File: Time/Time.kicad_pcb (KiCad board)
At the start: 2 copper layers, 100 x 100 mm, 24 parts, among them J1 Buss, J2 Timers, SW1 Slot, U1 DS12885, U2 74LS573, U3 74LS245, U4 GAL22V10, U5 74LS85, U6 MC6840, Y1 32.768KHz/6pF, Y2 32.768KHz

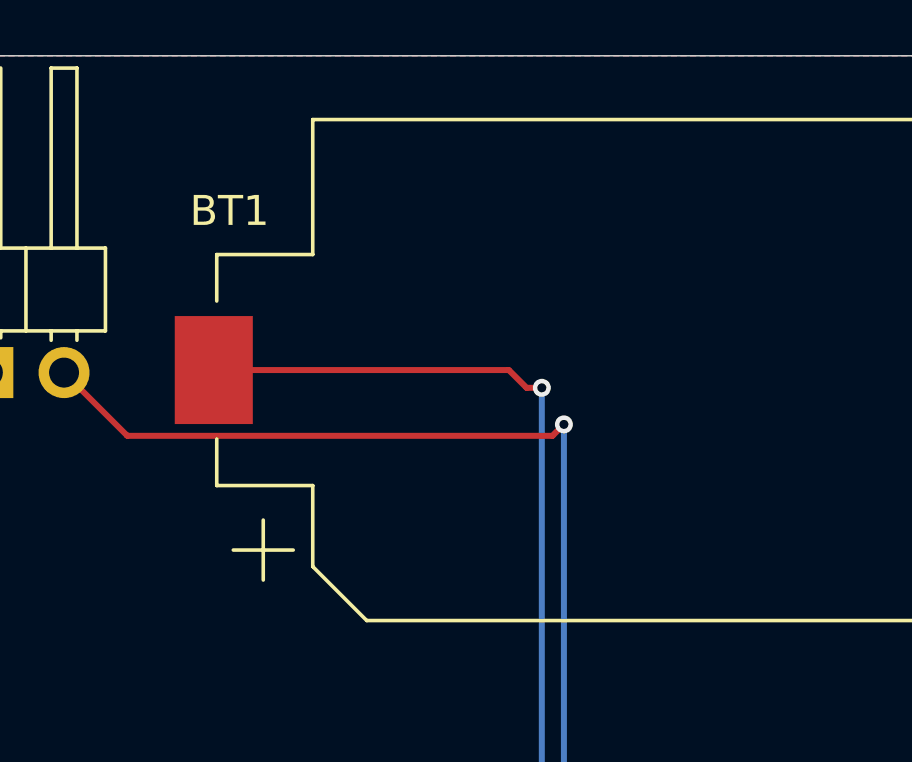
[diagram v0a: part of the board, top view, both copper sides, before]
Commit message: finish routing the coms board. add some step models to look at this thing in freecad
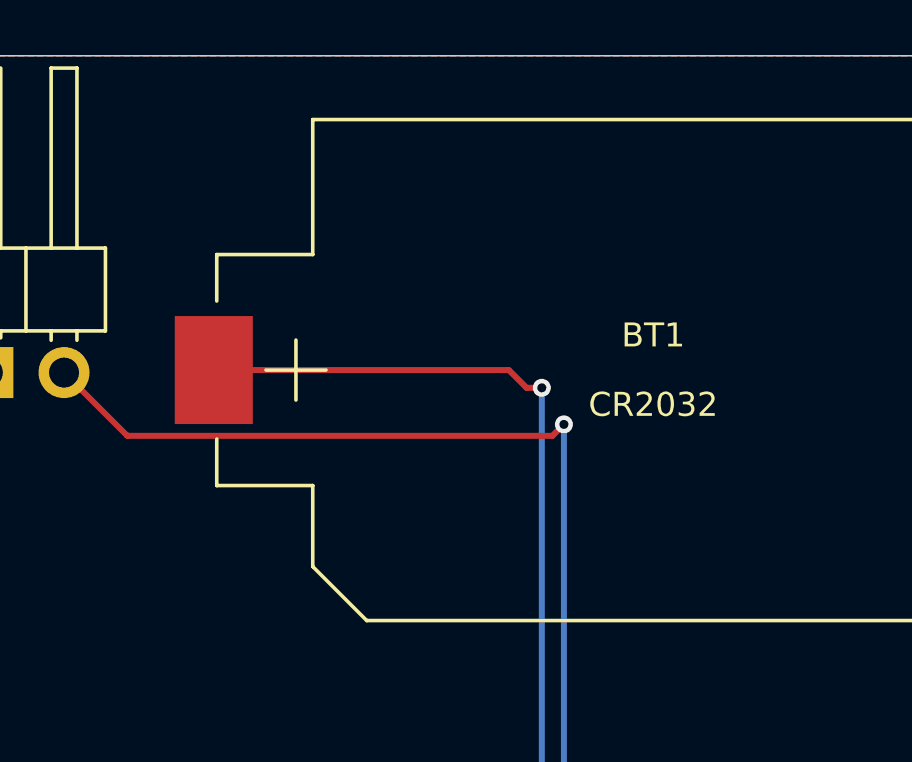
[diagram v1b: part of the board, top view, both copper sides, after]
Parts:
- BT1: footprint Battery:BatteryHolder_Keystone_1060_1x2032 -> 0-Footprints:BatteryHolder_Keystone_1060_1x2032

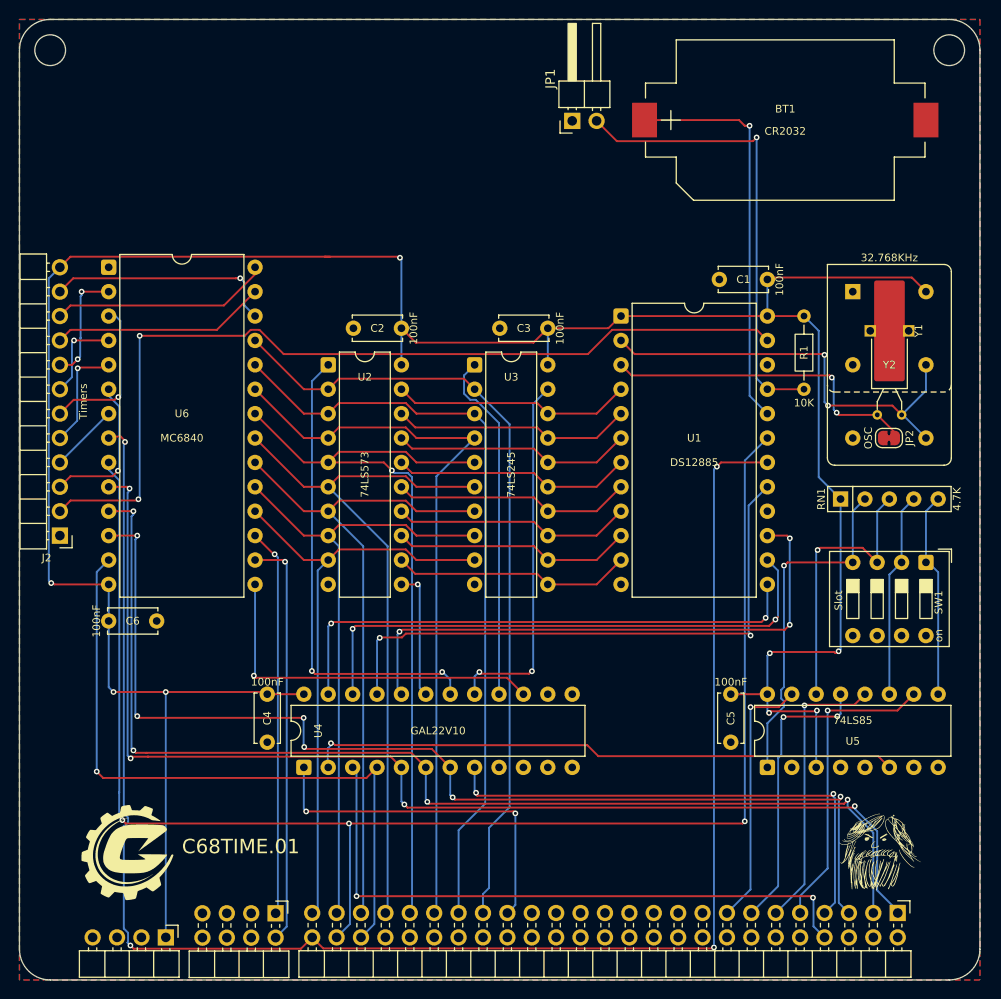
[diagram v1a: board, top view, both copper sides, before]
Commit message: added a bunch of debugging to emu, fixed a pile of translation issues on mikbug2. more to go
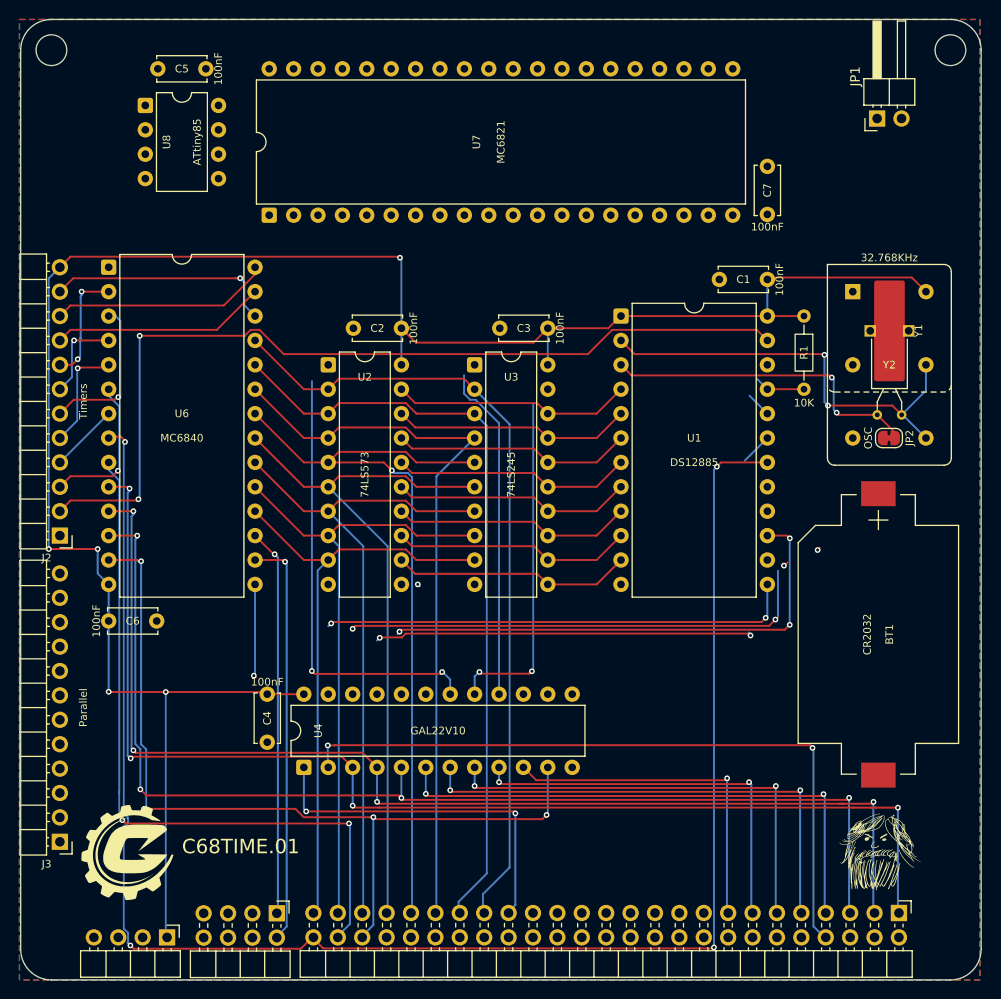
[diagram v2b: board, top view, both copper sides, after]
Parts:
- removed RN1: 4.7K, 0-Footprints:R_Array_SIP5
- removed SW1: Slot, 0-Footprints:SW_DIP_SPSTx04_Slide_9.78x12.34mm_W7.62mm_P2.54mm
- removed U5: 74LS85, 0-Footprints:DIP-16_W7.62mm
- added C7: 100nF, 0-Footprints:C_Disc_D5.0mm_W2.5mm_P5.00mm, F.Cu at (102.9, 40.3)
- added J3: Parallel, 0-Footprints:PinHeader_1x12_P2.54mm_Horizontal, F.Cu at (29.2, 110.6)
- added U7: MC6821, 0-Footprints:DIP-40_W15.24mm, F.Cu at (51.0, 45.4)
- added U8: ATtiny85, 0-Footprints:DIP-8_W7.62mm, F.Cu at (38.1, 34.0)
- moved C5 92.1 mm to (39.4, 30.1), turned to 0 degrees
- moved BT1 54.4 mm to (114.4, 89.0), turned to -90 degrees
- moved JP1 31.7 mm to (114.3, 35.3)
- moved J1 0.13 mm to (25.1, 25.0)
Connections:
- U1 pad 13: /~{RTC_CS} -> GND
- U1 pad 14: /RTC_AS -> /~{RTC_ADDR_SEL}
- U1 pad 15: /RTC_R/~{W} -> /R/~{W}
- U1 pad 17: /RTC_DS -> /~{RTC_DATA_SEL}
- U2 pad 1: /~{RTC_LATCH_CE} -> /~{RTC_ADDR_SEL}
- U2 pad 11: /~{RTC_LATCH_LE} -> /~{RTC_ADDR_SEL}
- U3 pad 1: /~{RTC_XCVR_DIR} -> /W/~{R}
- U3 pad 19: /~{RTC_XCVR_CE} -> /~{RTC_DATA_SEL}
- U4 pad 10: GND -> /A7
- U4 pad 11: GND -> /R/~{W}
- U4 pad 15: /~{PTM_CS} -> GND
- U4 pad 16: /~{RTC_XCVR_DIR} -> GND
- U4 pad 17: /~{RTC_XCVR_CE} -> GND
- U4 pad 18: /~{RTC_LATCH_CE} -> GND
- U4 pad 19: /~{RTC_LATCH_LE} -> /W/~{R}
- U4 pad 2: /SLOT_SEL -> /~{IO_SEL}
- U4 pad 20: /RTC_R/~{W} -> /~{PIA_SEL}
- U4 pad 21: /RTC_DS -> /~{PTM_SEL}
- U4 pad 22: /RTC_AS -> /~{RTC_DATA_SEL}
- U4 pad 23: /~{RTC_CS} -> /~{RTC_ADDR_SEL}
- U4 pad 3: /~{IO_SEL} -> /A0
- U4 pad 4: /R/~{W} -> /A1
- U4 pad 5: /A0 -> /A2
- U4 pad 6: /A1 -> /A3
- U4 pad 7: /A2 -> /A4
- U4 pad 8: /A3 -> /A5
- U4 pad 9: GND -> /A6
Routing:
- net GND: track 0.00 -> 167.2 mm, vias 0 -> 6
- net (no net): track 0.00 -> 91.1 mm, vias 0 -> 7
- net /~{IRQ}: track 156.2 -> 77.4 mm, vias 3 -> 2
- net /R/~{W}: track 70.4 -> 143.0 mm, vias 1 -> 7
- net +5V: track 277.2 -> 211.3 mm, vias 8 -> 5
- net /SLOT_SEL: track 61.8 -> 0.00 mm, vias 1 -> 0
- net /RTC_DS: track 61.3 -> 0.00 mm, vias 2 -> 0
- net /RTC_R/~{W}: track 58.7 -> 0.00 mm, vias 3 -> 0
- net /RTC_AS: track 58.4 -> 0.00 mm, vias 2 -> 0
- net /~{RTC_CS}: track 56.5 -> 0.00 mm, vias 2 -> 0
- net /~{RTC_LATCH_CE}: track 49.0 -> 0.00 mm, vias 2 -> 0
- net Net-(JP1-B): track 48.2 -> 5.39 mm, vias 1 -> 0
- net Net-(BT1-+): track 41.9 -> 2.62 mm, vias 1 -> 0
- net /~{RTC_XCVR_CE}: track 38.2 -> 0.00 mm, vias 2 -> 0
- net /~{RTC_XCVR_DIR}: track 36.6 -> 0.00 mm
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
